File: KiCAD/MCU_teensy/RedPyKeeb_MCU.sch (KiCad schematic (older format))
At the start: 8 parts, among them J0 Conn_01x04, J1 Conn_02x20_Top_Bottom, J2 Conn_01x04, U0 Teensy4.1, U1 TXS0104ED

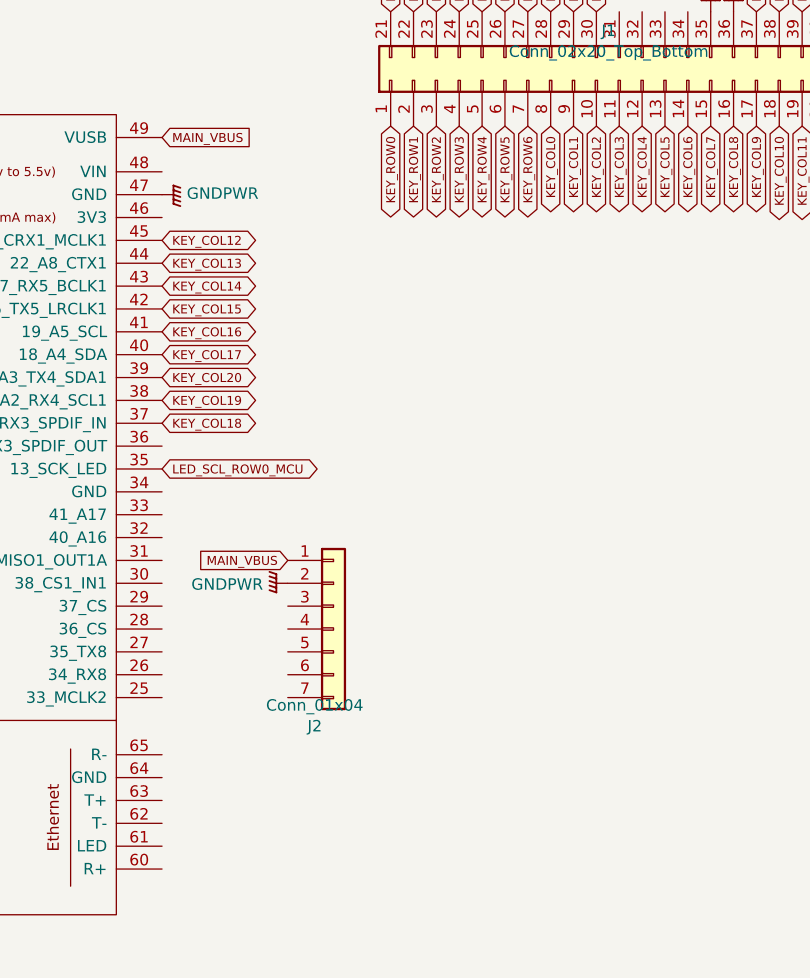
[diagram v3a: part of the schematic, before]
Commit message: Add dip switch to allow for plug-in/boot time option selects. Add status light LEDs to be handled and actually reflect capslock and numlock status. Add tiny debounce which is enough on my prototype board to remove false-positive key registration on the first column.
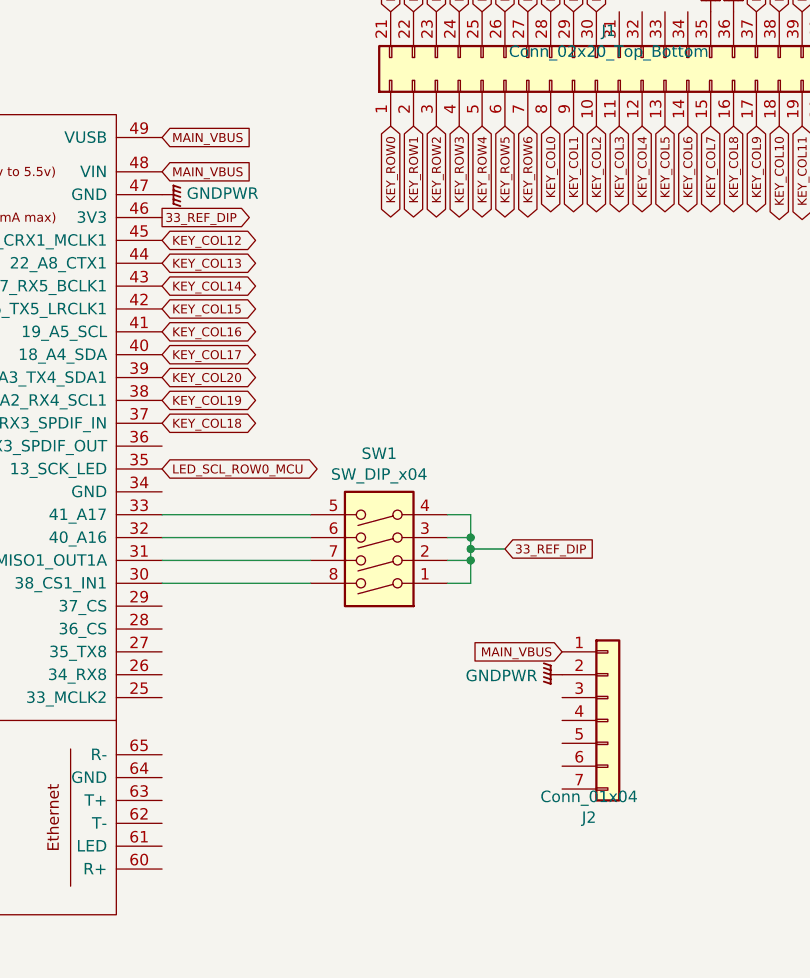
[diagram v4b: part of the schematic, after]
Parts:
- added SW1: SW_DIP_x04, Buttons_Switches_SMD:SW_DIP_x4_W8.61mm_Slide_LowProfile, symbol Switch:SW_DIP_x04
- C1, C2: Mfr No (none) -> 0805B101K100CT
- J0, J2: Mfr No (none) -> 3955
- J1: Mfr No (none) -> 95278-102-40LF
- R1: Mfr No (none) -> ERJ-6RED2003V
- U0: Mfr No (none) -> DEV-16771
- U1: Mfr No (none) -> TXS0104ED
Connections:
- net MAIN_VBUS: now also U0.48 (VIN)
- net at U0.30 (38_CS1_IN1): now also SW1.8
- net at U0.31 (39_MISO1_OUT1A): now also SW1.7
- net at U0.32 (40_A16): now also SW1.6
- net at U0.33 (41_A17): now also SW1.5
- net 33_REF_DIP: now reaches U0.46 (3V3)
- net 33_REF_DIP: now also SW1.1, SW1.2, SW1.3, SW1.4
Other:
- moved on the sheet: J2
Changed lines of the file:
@@
 Text Notes 950  1100 0    59   ~ 0
 TODO: Power bus needs to be sorted, see Unified-Daughterboard?
-Text GLabel 7300 1800 2    39   Input ~ 0
+Text GLabel 7300 1950 2    39   Input ~ 0
 MAIN_VBUS
 Text GLabel 5100 3250 0    39   BiDi ~ 0
@@
 F 4 "485-3955" H 6750 1000 50  0001 C CNN "Mouser No"
 F 5 "1528-2751-ND" H 6750 1000 50  0001 C CNN "Digikey Part No"
+F 6 "3955" H 6750 1000 50  0001 C CNN "Mfr No"
 	1    6750 1000
 	-1   0    0    1
@@
 L Connector_Generic:Conn_01x07 J2
 U 1 1 60E13064
-P 8050 3950
-F 0 "J2" H 7968 3525 50  0000 C CNN
-F 1 "Conn_01x04" H 7968 3616 50  0000 C CNN
-F 2 "Connector_JST:JST_EH_S7B-EH_1x07_P2.50mm_Horizontal" H 8050 3950 50  0001 C CNN
-F 3 "" H 8050 3950 50  0001 C CNN
-F 4 "485-3955" H 8050 3950 50  0001 C CNN "Mouser No"
-F 5 "1528-2751-ND" H 8050 3950 50  0001 C CNN "Digikey Part No"
-	1    8050 3950
+P 9250 4350
+F 0 "J2" H 9168 3925 50  0000 C CNN
+F 1 "Conn_01x04" H 9168 4016 50  0000 C CNN
+F 2 "Connector_JST:JST_EH_S7B-EH_1x07_P2.50mm_Horizontal" H 9250 4350 50  0001 C CNN
+F 3 "" H 9250 4350 50  0001 C CNN
+F 4 "485-3955" H 9250 4350 50  0001 C CNN "Mouser No"
+F 5 "1528-2751-ND" H 9250 4350 50  0001 C CNN "Digikey Part No"
+F 6 "3955" H 9250 4350 50  0001 C CNN "Mfr No"
+	1    9250 4350
 	1    0    0    -1
 $EndComp
@@
 F 3 "~" H 9200 1550 50  0001 C CNN
 F 4 "649-95278-102-40LF" H 9200 1550 50  0001 C CNN "Mouser No"
+F 5 "95278-102-40LF" H 9200 1550 50  0001 C CNN "Mfr No"
 	1    9200 1550
 	0    -1   -1   0
@@
 F 5 "TXS0104ED" H 2650 2900 50  0001 C CNN "element14 code"
 F 6 "296-34699-5-ND" H 2650 2900 50  0001 C CNN "Digikey Part No"
+F 7 "TXS0104ED" H 2650 2900 50  0001 C CNN "Mfr No"
 	1    2650 2900
 	-1   0    0    1
@@
 F 4 "791-0805B101K100CT" H 3300 3700 50  0001 C CNN "Mouser No"
 F 5 "1856401" H 3300 3700 50  0001 C CNN "element14 code"
+F 6 "0805B101K100CT" H 3300 3700 50  0001 C CNN "Mfr No"
 	1    3300 3700
 	0    1    1    0
@@
 F 4 "791-0805B101K100CT" H 2200 3700 50  0001 C CNN "Mouser No"
 F 5 "1856401" H 2200 3700 50  0001 C CNN "element14 code"
+F 6 "0805B101K100CT" H 2200 3700 50  0001 C CNN "Mfr No"
 	1    2200 3700
 	0    -1   -1   0
@@
 F 3 "" H 5800 4500 50  0001 C CNN
 F 4 "474-DEV-16771" H 6200 4100 50  0001 C CNN "Mouser No"
+F 5 "DEV-16771" H 6200 4100 50  0001 C CNN "Mfr No"
 	1    6200 4100
 	1    0    0    -1
@@
 Text GLabel 10100 1250 1    39   BiDi ~ 0
 LED_SDA_STATUS0
-Text GLabel 7850 3650 0    39   Input ~ 0
+Text GLabel 9050 4050 0    39   Input ~ 0
 MAIN_VBUS
 $Comp
 L power:GNDPWR #PWR0102
 U 1 1 60ACEAB9
-P 7850 3750
-F 0 "#PWR0102" H 7850 3550 50  0001 C CNN
-F 1 "GNDPWR" V 7855 3642 50  0000 R CNN
-F 2 "" H 7850 3700 50  0001 C CNN
-F 3 "" H 7850 3700 50  0001 C CNN
-	1    7850 3750
+P 9050 4150
+F 0 "#PWR0102" H 9050 3950 50  0001 C CNN
+F 1 "GNDPWR" V 9055 4042 50  0000 R CNN
+F 2 "" H 9050 4100 50  0001 C CNN
+F 3 "" H 9050 4100 50  0001 C CNN
+	1    9050 4150
 	0    1    1    0
 $EndComp
@@
 F 3 "~" H 3300 3400 50  0001 C CNN
 F 4 "667-ERJ-6RED2003V" H 3300 3400 50  0001 C CNN "Mouser No"
+F 5 "ERJ-6RED2003V" H 3300 3400 50  0001 C CNN "Mfr No"
 	1    3300 3400
 	0    1    1    0
@@
 	3200 3400 3050 3400
 Connection ~ 3200 3400
+Text GLabel 7300 1800 2    39   Input ~ 0
+MAIN_VBUS
+Text GLabel 7300 2150 2    39   Output ~ 0
+33_REF_DIP
+Text GLabel 8800 3600 2    39   Input ~ 0
+33_REF_DIP
+Wire Wire Line
+	8550 3750 8650 3750
+Wire Wire Line
+	8550 3650 8650 3650
+Connection ~ 8650 3650
+Wire Wire Line
+	8650 3650 8650 3750
+Wire Wire Line
+	8550 3550 8650 3550
+Connection ~ 8650 3550
+Wire Wire Line
+	8650 3550 8650 3600
+Wire Wire Line
+	8550 3450 8650 3450
+Wire Wire Line
+	8650 3450 8650 3550
+Wire Wire Line
+	8650 3600 8800 3600
+Connection ~ 8650 3600
+Wire Wire Line
+	8650 3600 8650 3650
+Wire Wire Line
+	7300 3450 7950 3450
+Wire Wire Line
+	7300 3550 7950 3550
+Wire Wire Line
+	7300 3650 7950 3650
+Wire Wire Line
+	7300 3750 7950 3750
+$Comp
+L Switch:SW_DIP_x04 SW1
+U 1 1 614F7E1F
+P 8250 3550
+F 0 "SW1" H 8250 3183 50  0000 C CNN
+F 1 "SW_DIP_x04" H 8250 3274 50  0000 C CNN
+F 2 "Buttons_Switches_SMD:SW_DIP_x4_W8.61mm_Slide_LowProfile" H 8250 3550 50  0001 C CNN
+F 3 "~" H 8250 3550 50  0001 C CNN
+F 4 "A6SN-4104" H 8250 3550 50  0001 C CNN "Mfr No"
+F 5 "653-A6SN-4104" H 8250 3550 50  0001 C CNN "Mouser No"
+	1    8250 3550
+	-1   0    0    1
+$EndComp
 $EndSCHEMATC

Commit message: Fix issues found with MCU and mainboard PCBs. Adding whatever fiddling I had with firmware.
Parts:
- J1: footprint Connector_PinSocket_2.54mm:PinSocket_2x20_P2.54mm_Vertical_SMD -> Custom_pico:PinHeader_2x20_P2.54mm_Vertical_SMD_doublesided
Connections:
- net KEY_COL18: now also U0.39 (17_A3_TX4_SDA1); no longer U0.37 (15_A1_RX3_SPDIF_IN)
- net KEY_COL20: now also U0.37 (15_A1_RX3_SPDIF_IN); no longer U0.39 (17_A3_TX4_SDA1)
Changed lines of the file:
@@
 Text GLabel 7300 2550 2    39   BiDi ~ 0
 KEY_COL15
-Text GLabel 7300 3050 2    39   BiDi ~ 0
+Text GLabel 7300 2850 2    39   BiDi ~ 0
 KEY_COL18
 Text GLabel 7300 2750 2    39   BiDi ~ 0
@@
 Text Notes 1900 1450 0    39   ~ 0
 0805B104K100CT for capacitors\n100nF
-Text GLabel 7300 2850 2    39   BiDi ~ 0
+Text GLabel 7300 3050 2    39   BiDi ~ 0
 KEY_COL20
 Text GLabel 5100 3350 0    39   Output ~ 0
@@
 F 0 "J1" V 9417 1496 50  0000 C CNN
 F 1 "Conn_02x20_Top_Bottom" V 9326 1496 50  0000 C CNN
-F 2 "Connector_PinSocket_2.54mm:PinSocket_2x20_P2.54mm_Vertical_SMD" H 9200 1550 50  0001 C CNN
+F 2 "Custom_pico:PinHeader_2x20_P2.54mm_Vertical_SMD_doublesided" H 9200 1550 50  0001 C CNN
 F 3 "~" H 9200 1550 50  0001 C CNN
 F 4 "649-95278-102-40LF" H 9200 1550 50  0001 C CNN "Mouser No"

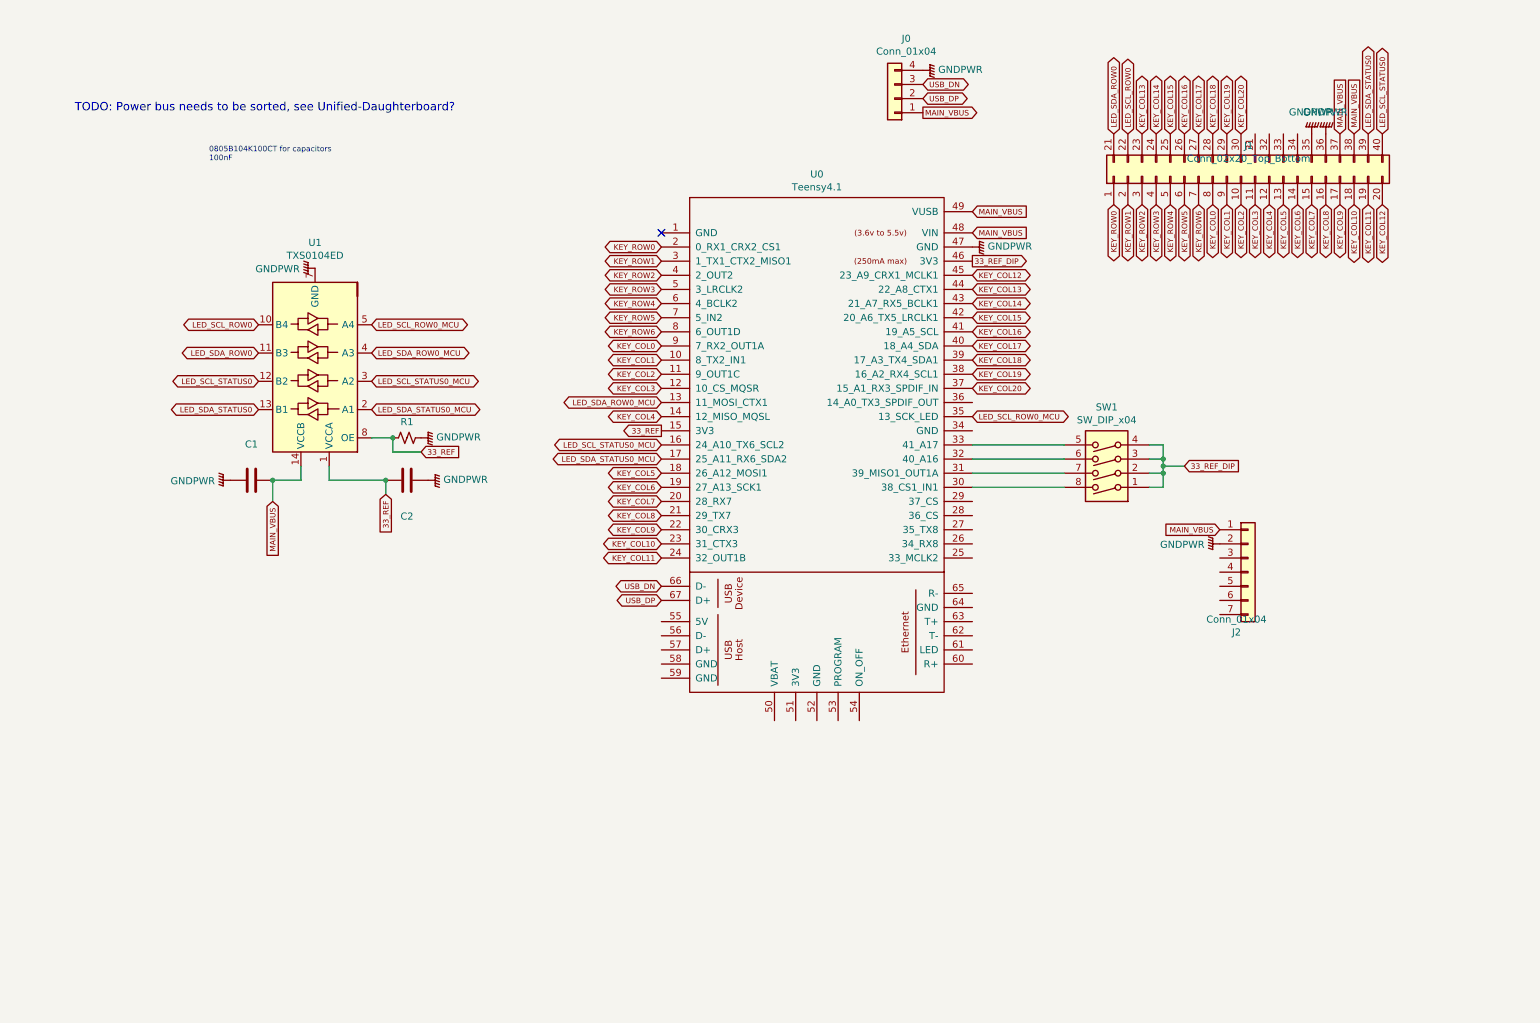
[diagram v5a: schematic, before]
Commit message: Make more fixes and revisions to both PCBs, add in a pico for lighting and display functions and hook up an SPI bus with key event data.
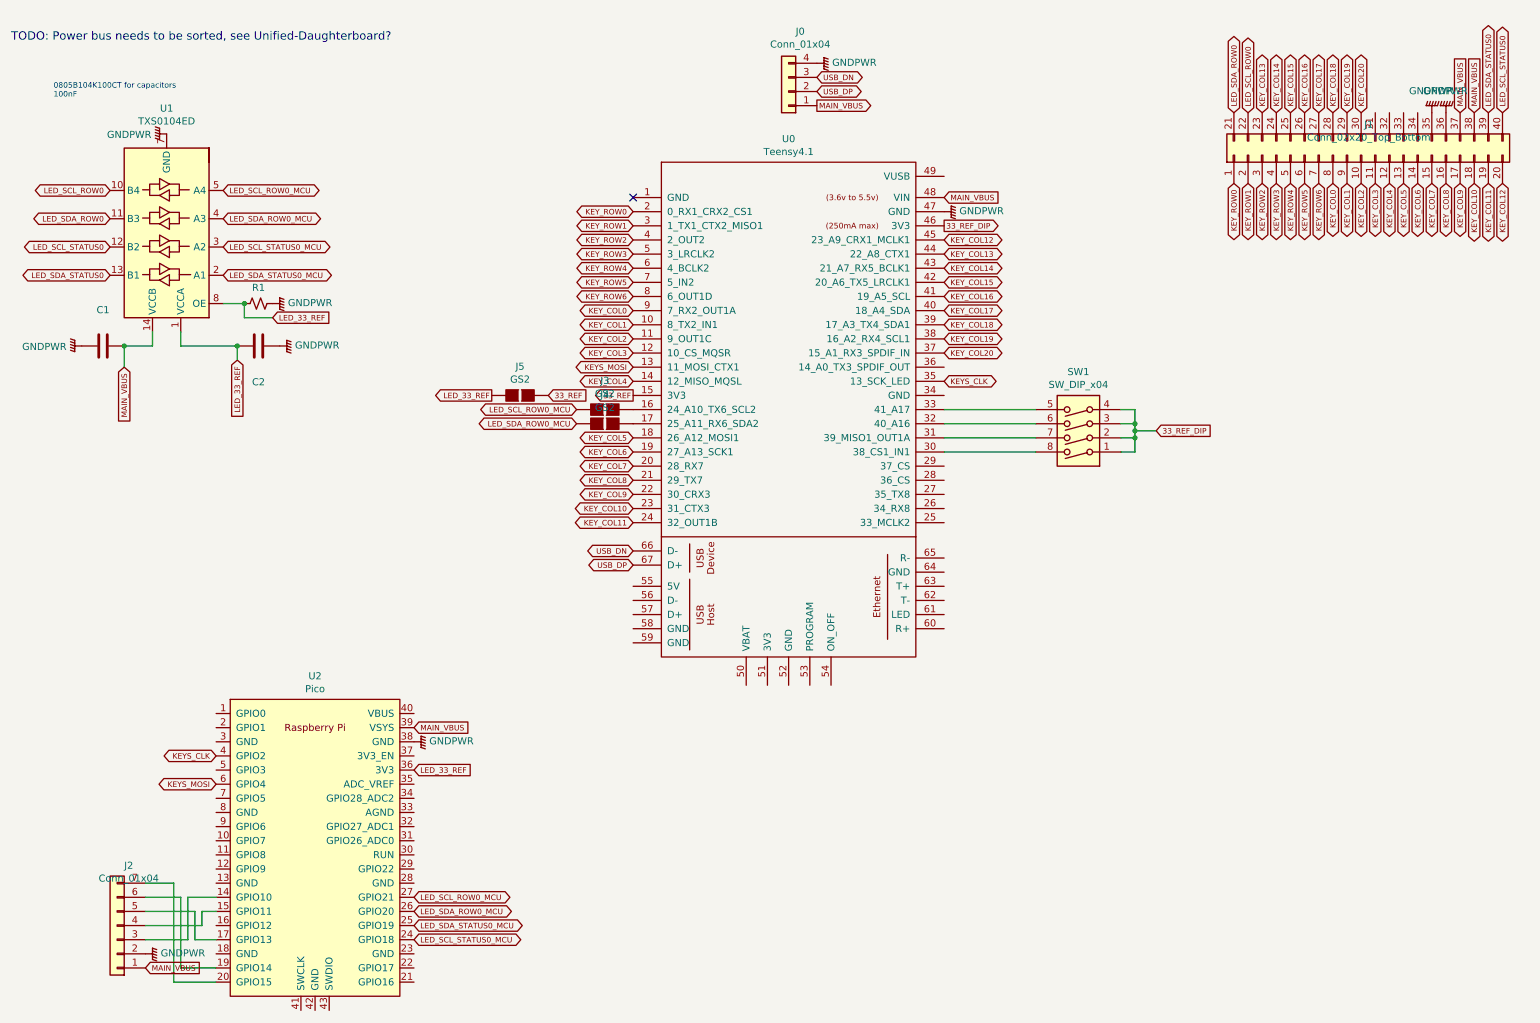
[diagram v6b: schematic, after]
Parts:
- added J3, J4, J5: GS2, Connectors:GS2, symbol conn:GS2
- added U2: Pico, Custom_pico:RPi_Pico_SMD_TH, symbol MCU_RaspberryPi_and_Boards:Pico
- SW1: footprint Buttons_Switches_SMD:SW_DIP_x4_W8.61mm_Slide_LowProfile -> Custom_pico:SW_DIP_x4_W8.61mm_Slide_LowProfile_bothsides
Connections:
- net 33_REF: now also J5.1 (G1); no longer C2.2, R1.2, U1.1 (VCCA), U1.8 (OE)
- net GNDPWR: now also U2.38 (GND)
- net LED_SCL_ROW0_MCU: now also J3.2 (G2), U2.27 (GPIO21); no longer U0.35 (13_SCK_LED)
- net LED_SCL_STATUS0_MCU: now also U2.24 (GPIO18); no longer U0.16 (24_A10_TX6_SCL2)
- net LED_SDA_ROW0_MCU: now also J4.2 (G2), U2.26 (GPIO20); no longer U0.13 (11_MOSI_CTX1)
- net LED_SDA_STATUS0_MCU: now also U2.25 (GPIO19); no longer U0.17 (25_A11_RX6_SDA2)
- net MAIN_VBUS: now also U2.39 (VSYS); no longer U0.49 (VUSB)
- net at J2.3 (Pin_3): now also U2.14 (GPIO10)
- net at J2.4 (Pin_4): now also U2.15 (GPIO11)
- net at J2.5 (Pin_5): now also U2.17 (GPIO13)
- net at J2.6 (Pin_6): now also U2.19 (GPIO14)
- net at J2.7 (Pin_7): now also U2.20 (GPIO15)
- new net: J3.1 (G1), U0.16 (24_A10_TX6_SCL2)
- new net: J4.1 (G1), U0.17 (25_A11_RX6_SDA2)
- new net KEYS_CLK: U0.35 (13_SCK_LED), U2.4 (GPIO2)
- new net KEYS_MOSI: U0.13 (11_MOSI_CTX1), U2.6 (GPIO4)
- new net LED_33_REF: C2.2, J5.2 (G2), R1.2, U1.1 (VCCA), U1.8 (OE), U2.36 (3V3)
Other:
- moved on the sheet: C1, C2, J0, J1, J2, R1, SW1, U0, U1
